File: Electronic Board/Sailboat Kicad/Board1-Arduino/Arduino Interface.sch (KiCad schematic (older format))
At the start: 0 parts

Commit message: Finished board-v0.1
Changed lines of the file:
@@
 F76 "53" B L 5700 5150 60
 F77 "51" B L 5700 5050 60
+F78 "5V_Sensors" B L 5700 1600 60
 $EndSheet
 Wire Wire Line
@@
 Wire Wire Line
 	4350 1600 3900 1600
+Wire Wire Line
+	4250 1500 4250 1800
+Wire Wire Line
+	4250 1800 5550 1800
+Wire Wire Line
+	5550 1800 5550 1600
+Wire Wire Line
+	5550 1600 5700 1600
+Connection ~ 4250 1500
 $EndSCHEMATC

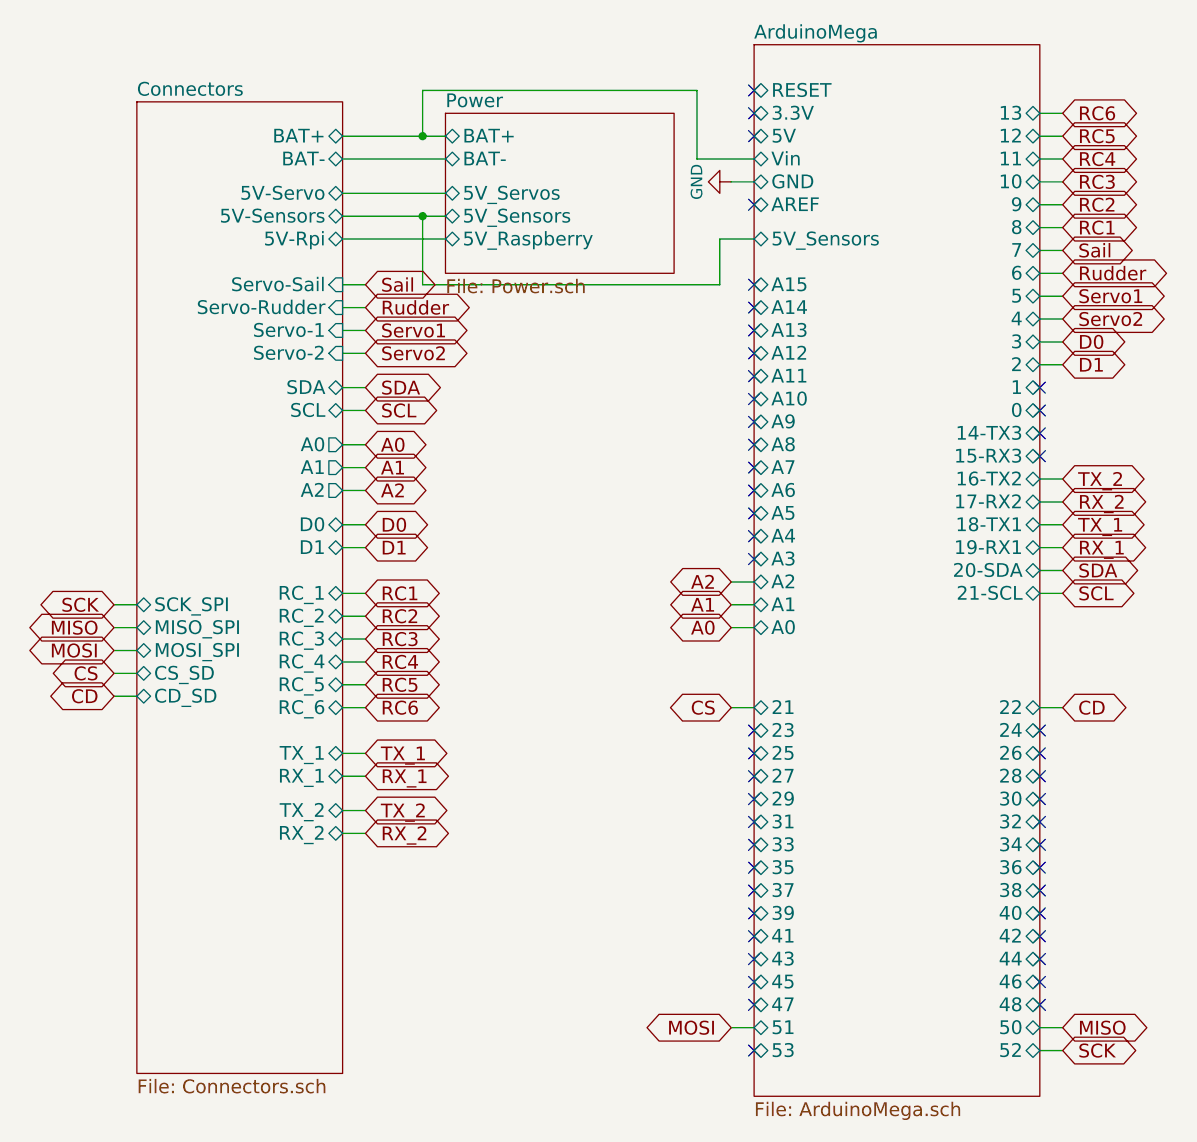
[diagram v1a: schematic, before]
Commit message: Cleaned up, and added security, text and better usability, preparation for board v2
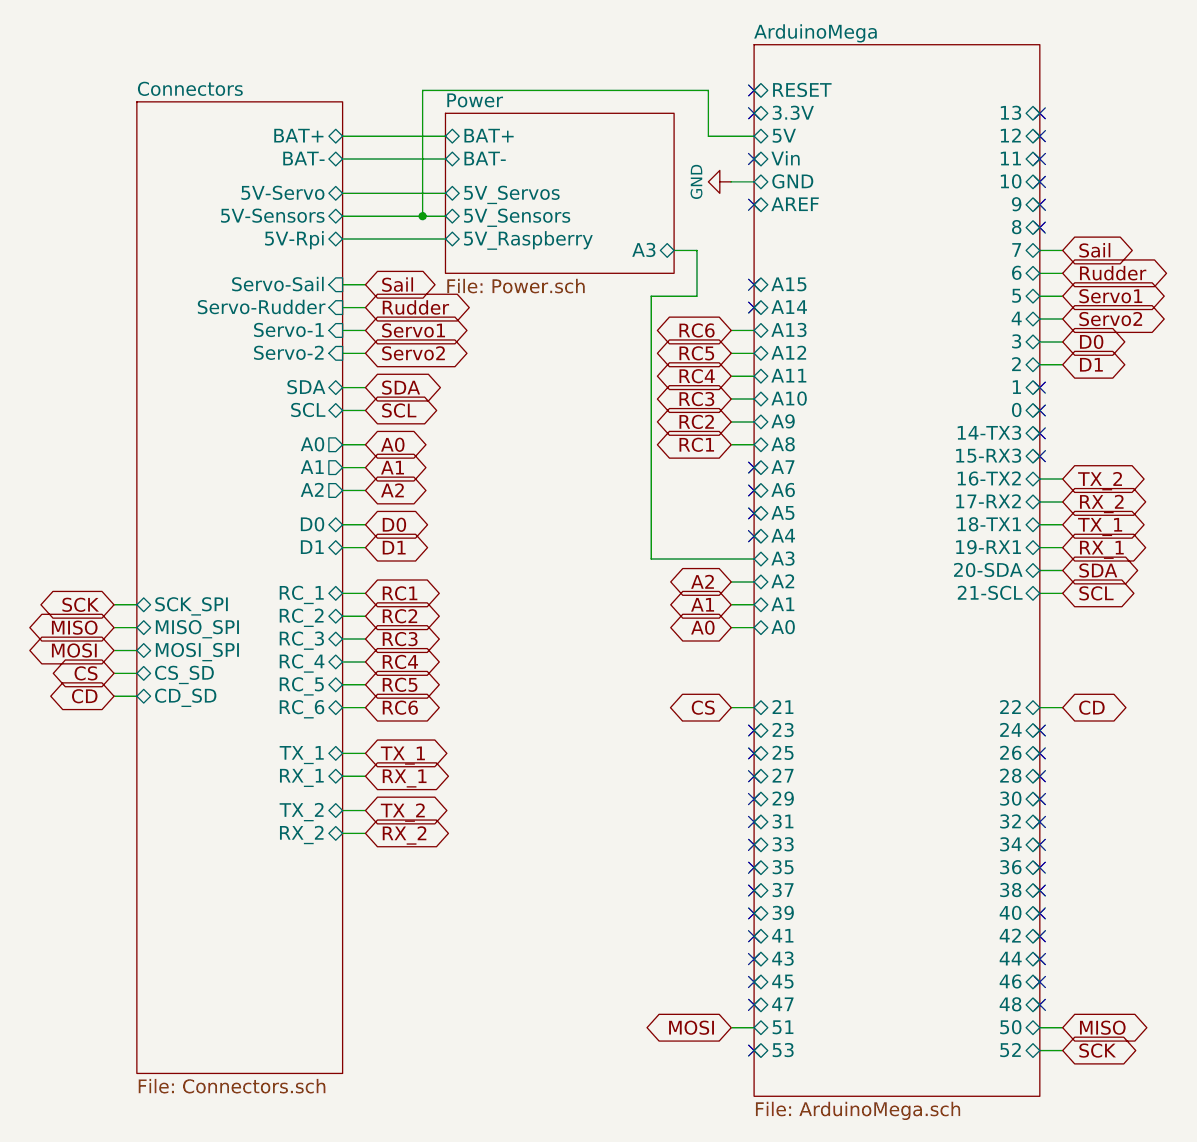
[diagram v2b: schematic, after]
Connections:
- no-connect marks 48 -> 47
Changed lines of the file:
@@
 F5 "5V_Raspberry" B L 4350 1600 60
 F6 "5V_Sensors" B L 4350 1500 60
+F7 "A3" B R 5350 1650 60
 $EndSheet
 $Sheet
@@
 F76 "53" B L 5700 5150 60
 F77 "51" B L 5700 5050 60
-F78 "5V_Sensors" B L 5700 1600 60
 $EndSheet
 Wire Wire Line
@@
 Wire Wire Line
 	4000 3650 3900 3650
-Text GLabel 7050 1550 2    60   BiDi ~ 0
+Text GLabel 5600 2500 0    60   BiDi ~ 0
 RC1
-Text GLabel 7050 1450 2    60   BiDi ~ 0
+Text GLabel 5600 2400 0    60   BiDi ~ 0
 RC2
-Text GLabel 7050 1350 2    60   BiDi ~ 0
+Text GLabel 5600 2300 0    60   BiDi ~ 0
 RC3
-Text GLabel 7050 1250 2    60   BiDi ~ 0
+Text GLabel 5600 2200 0    60   BiDi ~ 0
 RC4
-Text GLabel 7050 1150 2    60   BiDi ~ 0
+Text GLabel 5600 2100 0    60   BiDi ~ 0
 RC5
 Wire Wire Line
-	7050 1150 6950 1150
-Wire Wire Line
-	6950 1250 7050 1250
-Wire Wire Line
-	7050 1350 6950 1350
-Wire Wire Line
-	6950 1450 7050 1450
-Wire Wire Line
-	7050 1550 6950 1550
-Text GLabel 7050 1050 2    60   BiDi ~ 0
+	5700 2100 5600 2100
+Wire Wire Line
+	5600 2200 5700 2200
+Wire Wire Line
+	5700 2300 5600 2300
+Wire Wire Line
+	5600 2400 5700 2400
+Wire Wire Line
+	5700 2500 5600 2500
+Text GLabel 5600 2000 0    60   BiDi ~ 0
 RC6
 Wire Wire Line
-	7050 1050 6950 1050
+	5700 2000 5600 2000
 Text GLabel 4000 3850 2    60   BiDi ~ 0
 TX_1
@@
 NoConn ~ 5700 1800
 NoConn ~ 5700 1900
-NoConn ~ 5700 2000
-NoConn ~ 5700 2100
-NoConn ~ 5700 2200
-NoConn ~ 5700 2300
-NoConn ~ 5700 2400
-NoConn ~ 5700 2500
 NoConn ~ 5700 2600
 NoConn ~ 5700 2700
 NoConn ~ 5700 2800
 NoConn ~ 5700 2900
-NoConn ~ 5700 3000
 NoConn ~ 5700 3750
 NoConn ~ 5700 3850
@@
 NoConn ~ 5700 950
 NoConn ~ 5700 1050
-NoConn ~ 5700 1150
 NoConn ~ 5700 1450
 Text GLabel 2900 3200 0    60   BiDi ~ 0
@@
 	7050 3650 6950 3650
 Wire Wire Line
-	5700 1250 5450 1250
-Wire Wire Line
-	5450 1250 5450 950
-Wire Wire Line
-	5450 950  4250 950
-Wire Wire Line
-	4250 950  4250 1150
-Connection ~ 4250 1150
-Wire Wire Line
 	4350 1600 3900 1600
-Wire Wire Line
-	4250 1500 4250 1800
-Wire Wire Line
-	4250 1800 5550 1800
-Wire Wire Line
-	5550 1800 5550 1600
-Wire Wire Line
-	5550 1600 5700 1600
 Connection ~ 4250 1500
+NoConn ~ 6950 1050
+NoConn ~ 6950 1150
+NoConn ~ 6950 1250
+NoConn ~ 6950 1350
+NoConn ~ 6950 1450
+NoConn ~ 6950 1550
+NoConn ~ 5700 1250
+Wire Wire Line
+	5350 1650 5450 1650
+Wire Wire Line
+	5450 1650 5450 1850
+Wire Wire Line
+	5450 1850 5250 1850
+Wire Wire Line
+	5250 1850 5250 3000
+Wire Wire Line
+	5250 3000 5700 3000
+Wire Wire Line
+	4250 1500 4250 950
+Wire Wire Line
+	4250 950  5500 950
+Wire Wire Line
+	5500 950  5500 1150
+Wire Wire Line
+	5500 1150 5700 1150
 $EndSCHEMATC

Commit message: Updated version of Kicad, rendered images and BOM
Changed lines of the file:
@@
-EESchema Schematic File Version 2
-LIBS:power
-LIBS:device
-LIBS:switches
-LIBS:relays
-LIBS:motors
-LIBS:transistors
-LIBS:conn
-LIBS:linear
-LIBS:regul
-LIBS:74xx
-LIBS:cmos4000
-LIBS:adc-dac
-LIBS:memory
-LIBS:xilinx
-LIBS:microcontrollers
-LIBS:dsp
-LIBS:microchip
-LIBS:analog_switches
-LIBS:motorola
-LIBS:texas
-LIBS:intel
-LIBS:audio
-LIBS:interface
-LIBS:digital-audio
-LIBS:philips
-LIBS:display
-LIBS:cypress
-LIBS:siliconi
-LIBS:opto
-LIBS:atmel
-LIBS:contrib
-LIBS:valves
+EESchema Schematic File Version 4
 LIBS:Arduino Interface-cache
-EELAYER 25 0
+EELAYER 26 0
 EELAYER END
 $Descr A4 11693 8268
@@
 	3900 1250 4350 1250
 $Comp
-L GND #PWR01
+L power:GND #PWR01
 U 1 1 5A10358B
 P 5600 1350
@@
 	4000 1800 3900 1800
 Wire Wire Line
-	4350 1500 3900 1500
+	4350 1500 4250 1500
 Text GLabel 7050 1650 2    60   BiDi ~ 0
 Sail
@@
 Wire Wire Line
 	5500 1150 5700 1150
+Wire Wire Line
+	4250 1500 3900 1500
 $EndSCHEMATC
